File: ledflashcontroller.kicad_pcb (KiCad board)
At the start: 2 copper layers, 100 x 100 mm, 68 parts, among them J1 Conn_02x08_Odd_Even, J2 CONN_01X02, J3 CONN_01X02, K1 LDD-1000H, K2 LDD-1000H, P1 V_IN, P10 BNC, P11 BNC, P12 BNC, P2 I2C_HEADER, P3 GPIO_HEADER, P4 V_DIM1, P5 V_DIM2, P6 V_OUT, P7 BNC, P8 BNC, P9 BNC, Q1 IRLML6244, Q2 IRFB3256, U1 Teensy3.6, U10 DMC2700, U2 ISO1540, U3 DMC2700, U4 DMC2700, U5 ISO1540, U6 DMC2700, U7 DMC2700, U8 ISO1540, U9 DMC2700

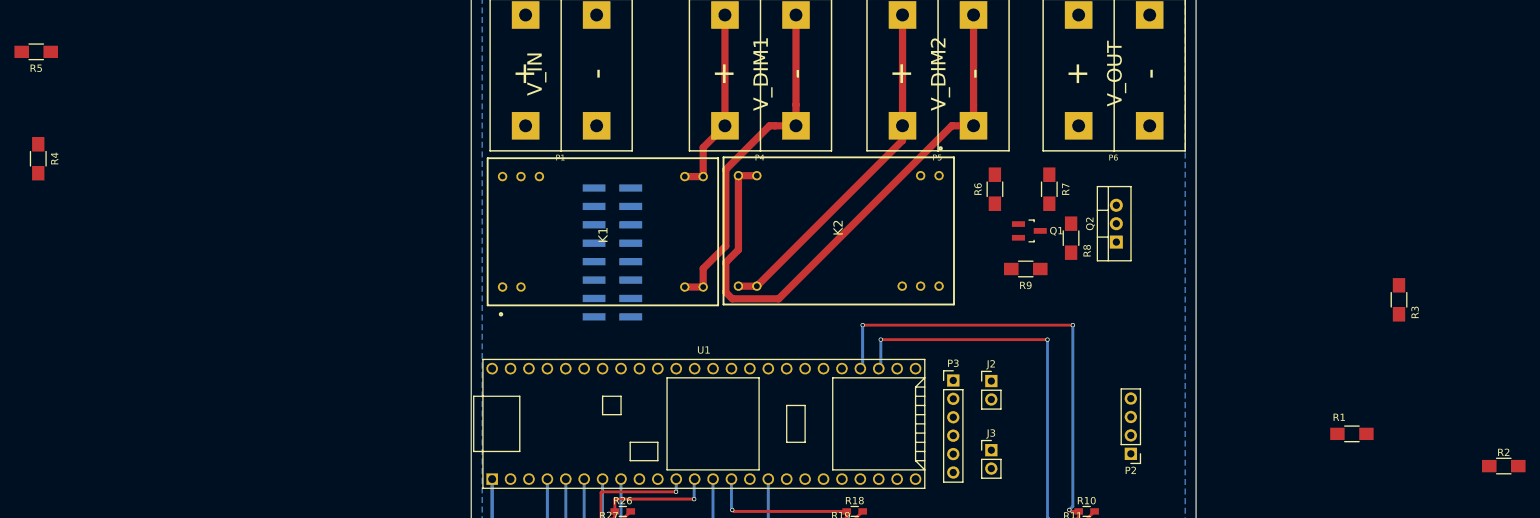
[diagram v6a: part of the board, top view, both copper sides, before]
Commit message: Arranged components so that they are close to their respective circuits
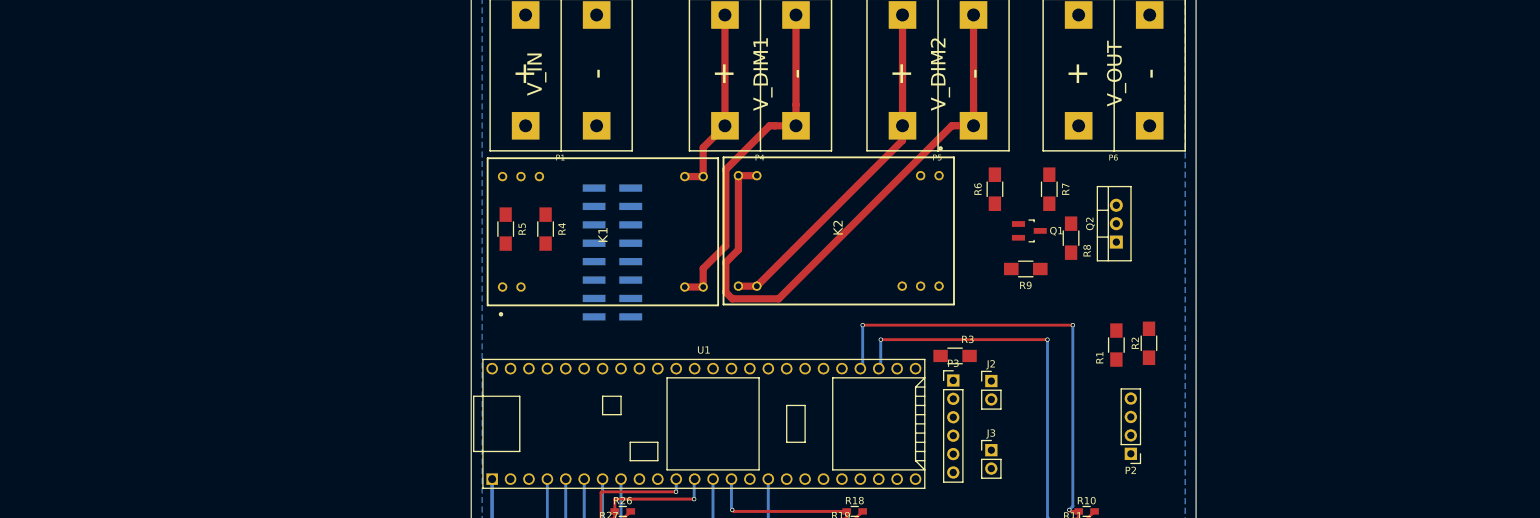
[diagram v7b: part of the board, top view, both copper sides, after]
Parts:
- moved R4 70.7 mm to (40.2, 61.8)
- moved R5 69.2 mm to (34.8, 61.8), turned to 270 degrees
- moved R3 61.7 mm to (96.8, 79.2), turned to 180 degrees
- moved R2 51.8 mm to (123.5, 77.5), turned to 90 degrees
- moved R1 34.7 mm to (119.0, 77.8), turned to 270 degrees
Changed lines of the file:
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@@
     (aux_axis_origin 30 30)
     (grid_origin 130 130)
-    (visible_elements FFFDFFFF)
+    (visible_elements FFFEFFFF)
     (pcbplotparams
       (layerselection 0x01000_00000000)
@@
   )
   (module Resistors_SMD:R_1206_HandSoldering (layer F.Cu)
-    (at 158 71.5 90)
+    (at 96.75 79.25 180)
     (descr "Resistor SMD 1206, hand soldering")
     (tags "resistor 1206")
     (attr smd)
-    (fp_text reference R3 (at -1.75 2.25 90) (layer F.SilkS)
-      (effects (font (size 1 1) (thickness 0.15)))
-    )
-    (fp_text value 10k (at 1.5 2.3 90) (layer F.Fab)
-      (effects (font (size 1 1) (thickness 0.15)))
-    )
-    (fp_line (start -3.3 -1.2) (end 3.3 -1.2) (layer F.CrtYd) (width 0.05))
-    (fp_line (start -3.3 1.2) (end 3.3 1.2) (layer F.CrtYd) (width 0.05))
-    (fp_line (start -3.3 -1.2) (end -3.3 1.2) (layer F.CrtYd) (width 0.05))
-    (fp_line (start 3.3 -1.2) (end 3.3 1.2) (layer F.CrtYd) (width 0.05))
-    (fp_line (start 1 1.075) (end -1 1.075) (layer F.SilkS) (width 0.15))
-    (fp_line (start -1 -1.075) (end 1 -1.075) (layer F.SilkS) (width 0.15))
-    (pad 1 smd rect (at -2 0 90) (size 2 1.7) (layers F.Cu F.Paste F.Mask)
-      (net 9 +3V3))
-    (pad 2 smd rect (at 2 0 90) (size 2 1.7) (layers F.Cu F.Paste F.Mask)
-      (net 41 /CS1))
-    (model Resistors_SMD.3dshapes/R_1206_HandSoldering.wrl
-      (at (xyz 0 0 0))
-      (scale (xyz 1 1 1))
-      (rotate (xyz 0 0 0))
-    )
-  )
-  (module Resistors_SMD:R_1206_HandSoldering (layer F.Cu)
-    (at 151.5 90 180)
-    (descr "Resistor SMD 1206, hand soldering")
-    (tags "resistor 1206")
-    (attr smd)
-    (fp_text reference R1 (at 1.75 2.25 180) (layer F.SilkS)
-      (effects (font (size 1 1) (thickness 0.15)))
-    )
-    (fp_text value 4.7k (at -1.5 2.25 180) (layer F.Fab)
+    (fp_text reference R3 (at -1.75 2.25 180) (layer F.SilkS)
+      (effects (font (size 1 1) (thickness 0.15)))
+    )
+    (fp_text value 10k (at 1.5 2.3 180) (layer F.Fab)
       (effects (font (size 1 1) (thickness 0.15)))
     )
@@
     (fp_line (start -1 -1.075) (end 1 -1.075) (layer F.SilkS) (width 0.15))
     (pad 1 smd rect (at -2 0 180) (size 2 1.7) (layers F.Cu F.Paste F.Mask)
+      (net 9 +3V3))
+    (pad 2 smd rect (at 2 0 180) (size 2 1.7) (layers F.Cu F.Paste F.Mask)
+      (net 41 /CS1))
+    (model Resistors_SMD.3dshapes/R_1206_HandSoldering.wrl
+      (at (xyz 0 0 0))
+      (scale (xyz 1 1 1))
+      (rotate (xyz 0 0 0))
+    )
+  )
+  (module Resistors_SMD:R_1206_HandSoldering (layer F.Cu)
+    (at 119 77.75 270)
+    (descr "Resistor SMD 1206, hand soldering")
+    (tags "resistor 1206")
+    (attr smd)
+    (fp_text reference R1 (at 1.75 2.25 270) (layer F.SilkS)
+      (effects (font (size 1 1) (thickness 0.15)))
+    )
+    (fp_text value 4.7k (at -1.5 2.25 270) (layer F.Fab)
+      (effects (font (size 1 1) (thickness 0.15)))
+    )
+    (fp_line (start -3.3 -1.2) (end 3.3 -1.2) (layer F.CrtYd) (width 0.05))
+    (fp_line (start -3.3 1.2) (end 3.3 1.2) (layer F.CrtYd) (width 0.05))
+    (fp_line (start -3.3 -1.2) (end -3.3 1.2) (layer F.CrtYd) (width 0.05))
+    (fp_line (start 3.3 -1.2) (end 3.3 1.2) (layer F.CrtYd) (width 0.05))
+    (fp_line (start 1 1.075) (end -1 1.075) (layer F.SilkS) (width 0.15))
+    (fp_line (start -1 -1.075) (end 1 -1.075) (layer F.SilkS) (width 0.15))
+    (pad 1 smd rect (at -2 0 270) (size 2 1.7) (layers F.Cu F.Paste F.Mask)
       (net 11 /SDA))
-    (pad 2 smd rect (at 2 0 180) (size 2 1.7) (layers F.Cu F.Paste F.Mask)
+    (pad 2 smd rect (at 2 0 270) (size 2 1.7) (layers F.Cu F.Paste F.Mask)
       (net 9 +3V3))
     (model Resistors_SMD.3dshapes/R_1206_HandSoldering.wrl
@@
   )
   (module Resistors_SMD:R_1206_HandSoldering (layer F.Cu)
-    (at -29.74 52.04 270)
+    (at 40.25 61.75 270)
     (descr "Resistor SMD 1206, hand soldering")
     (tags "resistor 1206")
@@
   )
   (module Resistors_SMD:R_1206_HandSoldering (layer F.Cu)
-    (at -30.02 37.29 180)
+    (at 34.75 61.75 270)
     (descr "Resistor SMD 1206, hand soldering")
     (tags "resistor 1206")
     (attr smd)
-    (fp_text reference R5 (at 0 -2.3 180) (layer F.SilkS)
-      (effects (font (size 1 1) (thickness 0.15)))
-    )
-    (fp_text value 220 (at 0 2.3 180) (layer F.Fab)
+    (fp_text reference R5 (at 0 -2.3 270) (layer F.SilkS)
+      (effects (font (size 1 1) (thickness 0.15)))
+    )
+    (fp_text value 220 (at 0 2.3 270) (layer F.Fab)
       (effects (font (size 1 1) (thickness 0.15)))
     )
@@
     (fp_line (start 1 1.075) (end -1 1.075) (layer F.SilkS) (width 0.15))
     (fp_line (start -1 -1.075) (end 1 -1.075) (layer F.SilkS) (width 0.15))
-    (pad 1 smd rect (at -2 0 180) (size 2 1.7) (layers F.Cu F.Paste F.Mask)
+    (pad 1 smd rect (at -2 0 270) (size 2 1.7) (layers F.Cu F.Paste F.Mask)
       (net 6 "Net-(K2-Pad22)"))
-    (pad 2 smd rect (at 2 0 180) (size 2 1.7) (layers F.Cu F.Paste F.Mask)
+    (pad 2 smd rect (at 2 0 270) (size 2 1.7) (layers F.Cu F.Paste F.Mask)
       (net 15 /DIM2))
     (model Resistors_SMD.3dshapes/R_1206_HandSoldering.wrl
@@
   )
   (module Resistors_SMD:R_1206_HandSoldering (layer F.Cu)
-    (at 172.45 94.44)
+    (at 123.5 77.5 90)
     (descr "Resistor SMD 1206, hand soldering")
     (tags "resistor 1206")
     (attr smd)
-    (fp_text reference R2 (at 0 -1.85) (layer F.SilkS)
-      (effects (font (size 1 1) (thickness 0.15)))
-    )
-    (fp_text value 4.7k (at 0 1.9) (layer F.Fab)
-      (effects (font (size 1 1) (thickness 0.15)))
-    )
-    (fp_text user %R (at 0 0) (layer F.Fab)
+    (fp_text reference R2 (at 0 -1.85 90) (layer F.SilkS)
+      (effects (font (size 1 1) (thickness 0.15)))
+    )
+    (fp_text value 4.7k (at 0 1.9 90) (layer F.Fab)
+      (effects (font (size 1 1) (thickness 0.15)))
+    )
+    (fp_text user %R (at 0 0 90) (layer F.Fab)
       (effects (font (size 0.7 0.7) (thickness 0.105)))
     )
@@
     (fp_line (start 3.25 1.1) (end 3.25 -1.11) (layer F.CrtYd) (width 0.05))
     (fp_line (start 3.25 1.1) (end -3.25 1.1) (layer F.CrtYd) (width 0.05))
-    (pad 1 smd rect (at -2 0) (size 2 1.7) (layers F.Cu F.Paste F.Mask)
+    (pad 1 smd rect (at -2 0 90) (size 2 1.7) (layers F.Cu F.Paste F.Mask)
       (net 10 /SCL))
-    (pad 2 smd rect (at 2 0) (size 2 1.7) (layers F.Cu F.Paste F.Mask)
+    (pad 2 smd rect (at 2 0 90) (size 2 1.7) (layers F.Cu F.Paste F.Mask)
       (net 9 +3V3))
     (model ${KISYS3DMOD}/Resistors_SMD.3dshapes/R_1206.wrl

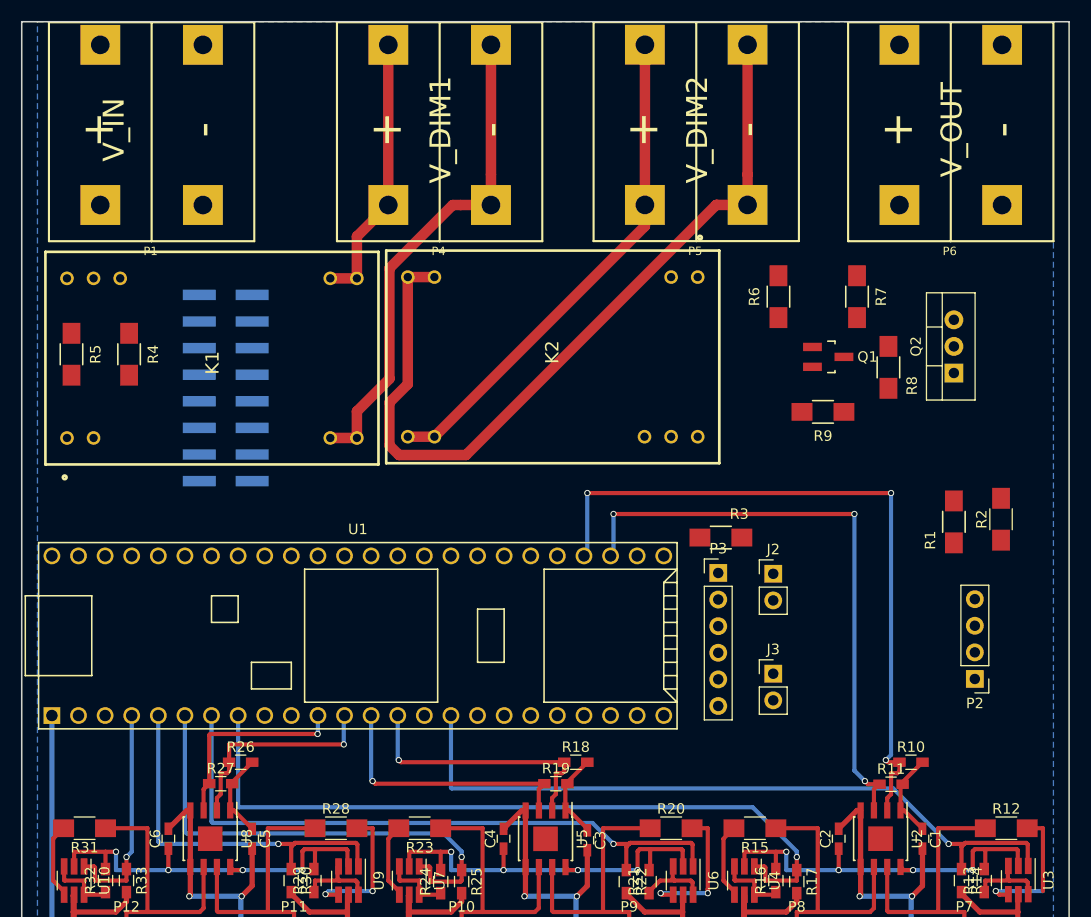
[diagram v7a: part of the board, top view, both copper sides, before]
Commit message: Bugfixes for vias to close to wires
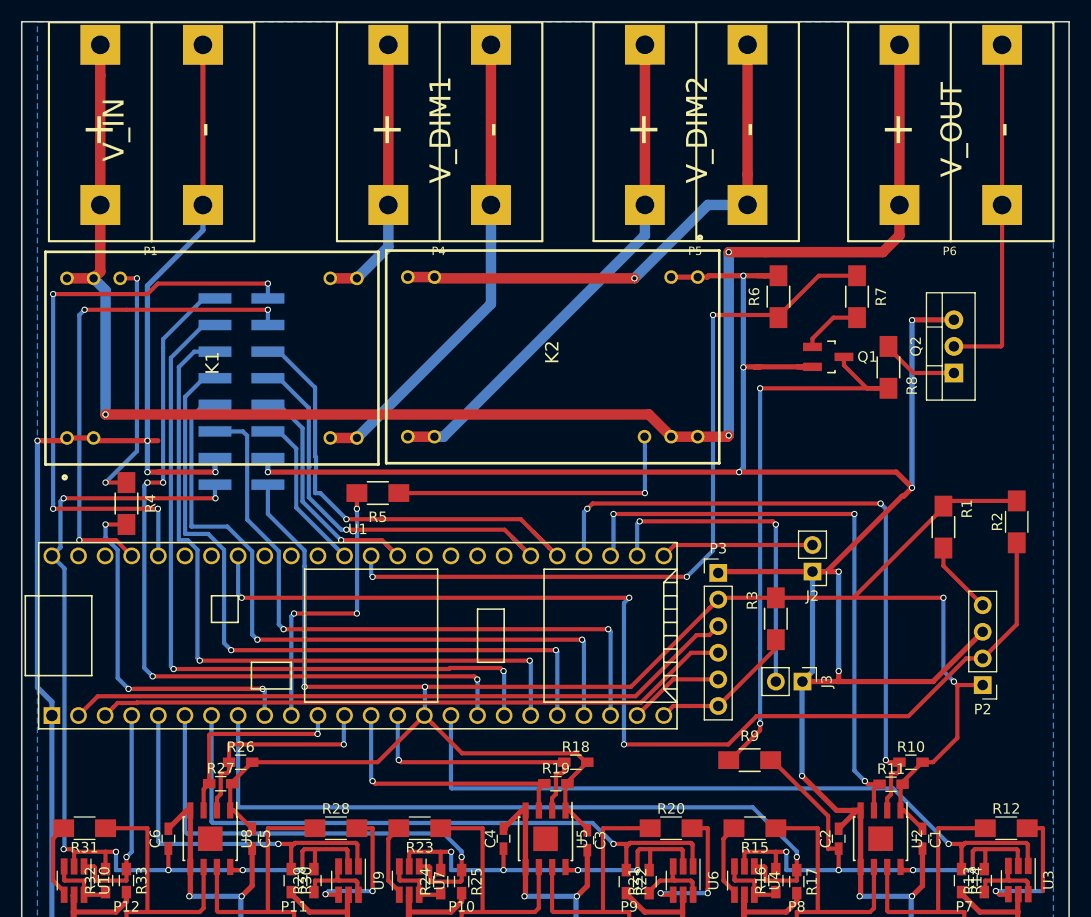
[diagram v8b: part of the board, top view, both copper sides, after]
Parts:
- moved R9 34.0 mm to (99.5, 100.5), turned to 0 degrees
- moved R5 32.1 mm to (64.0, 75.0), turned to 180 degrees
- moved R4 14.3 mm to (40.0, 76.0)
- moved R3 9.36 mm to (102.0, 87.0), turned to 270 degrees
- moved J2 3.76 mm to (105.5, 82.5), turned to 180 degrees
- moved J3 2.89 mm to (104.5, 93.0), turned to 270 degrees
- moved J1 1.54 mm to (51.0, 65.3)
- moved R2 1.52 mm to (125.0, 77.8)
- moved R1 1.12 mm to (118.0, 78.2), turned to 90 degrees
- moved P2 0.95 mm to (121.8, 93.3)
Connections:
- J1 pad 1: /TRIG_IO0 -> /TRIG_IO1
- J1 pad 11: /TRIG_IO11 -> /TRIG_IO0
- J1 pad 3: /TRIG_IO1 -> /TRIG_IO2
- J1 pad 5: /TRIG_IO2 -> /TRIG_IO10
- J1 pad 7: /TRIG_IO5 -> /TRIG_IO11
- J1 pad 9: /TRIG_IO10 -> /TRIG_IO5
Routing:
- net GND: track 432.6 -> 728.4 mm, vias 6 -> 19
- net +3V3: track 24.9 -> 190.0 mm, vias 0 -> 4
- net +48V: track 0.00 -> 151.7 mm, vias 0 -> 3
- net /SCL: track 0.00 -> 105.4 mm, vias 0 -> 3
- net /TRIG_PU6: track 0.00 -> 75.3 mm, vias 0 -> 4
- net /VOUT: track 0.00 -> 73.7 mm, vias 0 -> 3
- net /TRIG_PU8: track 0.00 -> 71.3 mm, vias 0 -> 2
- net /TRIG_PU7: track 0.00 -> 71.3 mm, vias 0 -> 2
- net /TRIG_PU9: track 0.00 -> 68.2 mm, vias 0 -> 2
- net /TRIG_PU10: track 0.00 -> 68.0 mm, vias 0 -> 2
- net /MOSI1: track 0.00 -> 64.6 mm
- net /TRIG_PU11: track 0.00 -> 63.6 mm, vias 0 -> 2
- net +5V: track 118.9 -> 182.2 mm, vias 12 -> 15
- net /MISO1: track 0.00 -> 61.0 mm
- net /TRIG_IO1: track 0.00 -> 57.4 mm, vias 0 -> 4
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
